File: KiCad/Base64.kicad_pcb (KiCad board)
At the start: 4 copper layers, 25.1 x 81.8 mm, 29 parts, among them J1 1473149-1, J2 Conn_01x03, U1 501MLFT, U10 68000_PinHeader, U2 SN74CBTD3861DGVR, U3 SN74CBTD3861DGVR, U4 SN74CBTD3861DGVR, U5 SN74CBTD3861DGVR, U6 SN74CBTD3861DGVR, U7 SN74CBTD3861DGVR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

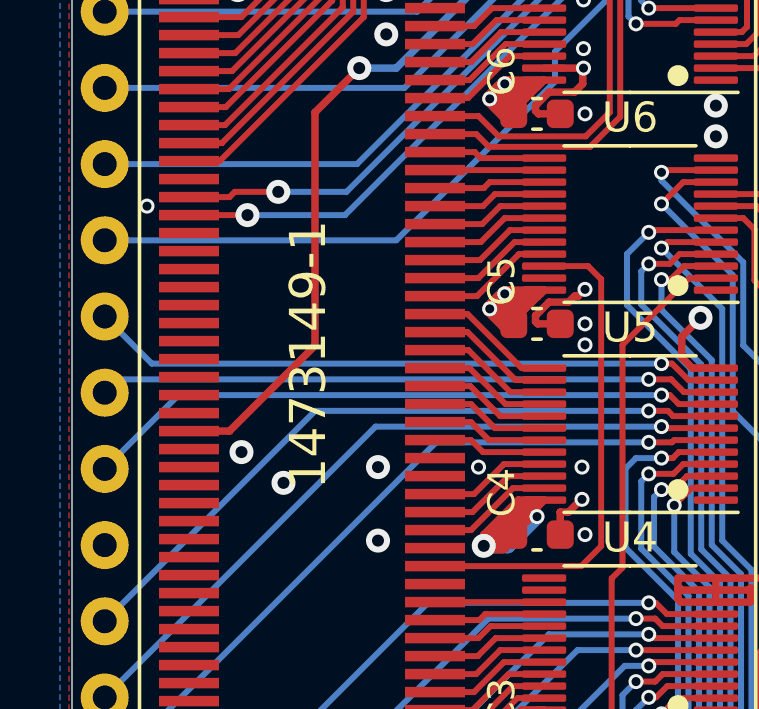
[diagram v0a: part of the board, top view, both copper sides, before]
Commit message: Change J1 value from 1473149-1 (SO-DIMM DDR) to 1473149-4 (SO-DIMM DDR2) as keying is different and iCESugar-Pro module is of DDR2 type.
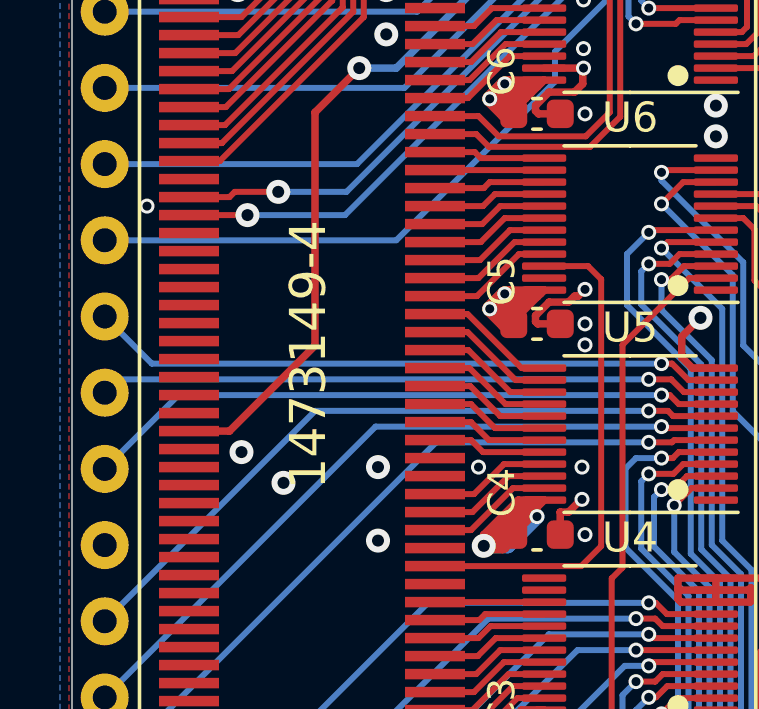
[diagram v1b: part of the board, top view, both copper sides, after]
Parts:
- J1: value 1473149-1 -> 1473149-4
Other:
- board text added: "1473149-4"
- board text removed: "1473149-1"
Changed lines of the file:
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@@
       (effects (font (size 1 1) (thickness 0.15)))
     )
-    (fp_text value 1473149-1 (at -5.6 0 90) (layer F.Fab) hide
+    (fp_text value 1473149-4 (at -5.6 0 90) (layer F.Fab) hide
       (effects (font (size 1 1) (thickness 0.15)))
     )
@@
     )
   )
-  (gr_text 1473149-1 (at 97.225 79.3 90) (layer F.SilkS)
+  (gr_text 1473149-4 (at 97.225 79.3 90) (layer F.SilkS)
     (effects (font (size 1.2 1.2) (thickness 0.2)))
   )

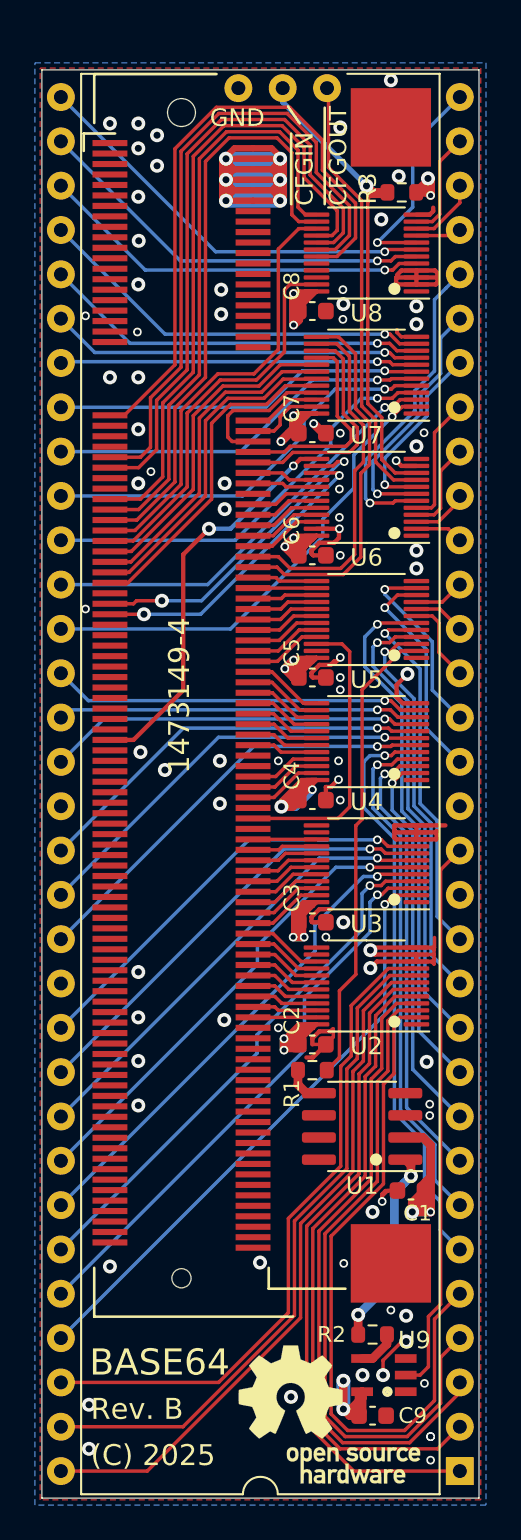
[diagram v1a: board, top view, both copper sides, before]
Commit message: Redesign with 570BLFT in order to generate a phase aligned 84 MHz clock
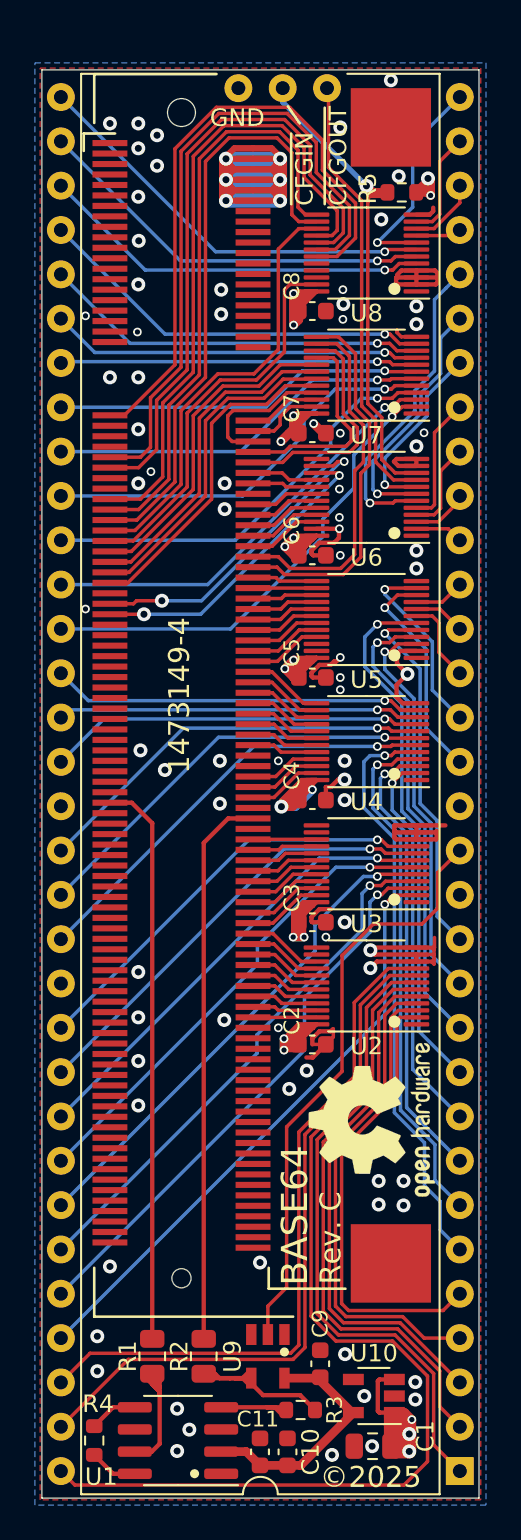
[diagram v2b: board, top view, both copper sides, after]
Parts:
- removed the REF** at (103.6, 120.5)
- added C10: 100nF, Capacitor_SMD:C_0603_1608Metric, F.Cu at (103.4, 122.7)
- added C11: 10nF, Capacitor_SMD:C_0603_1608Metric, F.Cu at (101.8, 122.7)
- added R3: 33, Resistor_SMD:R_0603_1608Metric, F.Cu at (104.2, 120.2)
- added R4: 33, Resistor_SMD:R_0603_1608Metric, F.Cu at (92.3, 122.0)
- added REF**: OSHW-Logo2_9.8x8mm_SilkScreen, Symbol:OSHW-Logo2_9.8x8mm_SilkScreen, F.Cu at (108.3, 103.6)
- added U10: TLV75533PDBVR, Package_TO_SOT_SMD:SOT-23-5, F.Cu at (108.4, 119.5)
- C1: value 10nF -> 1uF; footprint Capacitor_SMD:C_0603_1608Metric -> Capacitor_SMD:C_0805_2012Metric
- R1, R2: footprint Resistor_SMD:R_0603_1608Metric -> Resistor_SMD:R_0805_2012Metric
- U1: value 501MLFT -> 570BLFT
- U9: value 74AHCT1G17 -> SN74LVC1G17DBVR; footprint Base64:SOT95P275X110-5N -> Base64:SOT95P280X145-5N
- moved U1 20.9 mm to (97.2, 122.0)
- moved R1 18.8 mm to (95.7, 117.2), turned to 90 degrees
- moved C1 14.8 mm to (108.3, 122.3)
- moved R2 9.76 mm to (98.6, 117.2), turned to 270 degrees
- moved U9 6.74 mm to (102.3, 117.2), turned to 270 degrees
- moved C9 4.23 mm to (105.3, 117.6), turned to 90 degrees
- renumbered R3 to R5, U10 to U11
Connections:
- net Net-(U1-Pad6) renamed /S0
- C9 pad 1: VCC -> 3V3
- J1 pad 115: PL26A -> 12x_CLK
- J1 pad 118: PT27A -> CLK
- R1 pad 1: Net-(R1-Pad1) -> /CLKx12
- R1 pad 2: 2xCLK -> 12x_CLK
- R2 pad 1: /CLK_BUF -> CLK
- R2 pad 2: CLK -> /CLK_BUF
- U1 pad 1: CLK -> /S1
- U1 pad 2: VCC -> 3V3
- U1 pad 4: Net-(U1-Pad4) -> ICLK
- U1 pad 5: Net-(R1-Pad1) -> /FBIN
- U1 pad 7: Net-(U1-Pad7) -> /CLKx12
- U1 pad 8: Net-(U1-Pad8) -> /CLKx6
- U5 pad 2: 2xCLK -> GND
- U5 pad 22: PT27A -> Net-(U5-Pad22)
- U6 pad 11: CLK -> GND
- U6 pad 13: PL23A -> Net-(U6-Pad13)
- U9 pad 5: VCC -> 3V3
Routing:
- net 12x_CLK: track 0.00 -> 32.5 mm
- net 2xCLK: track 26.7 -> 0.00 mm
- net CLK: track 56.4 -> 31.8 mm, vias 3 -> 0
- net PL23A: track 23.1 -> 0.00 mm, vias 2 -> 0
- net D5: track 40.2 -> 57.4 mm
- net PT27A: track 16.8 -> 0.00 mm
- net 3V3: track 0.00 -> 14.1 mm
- net D0: track 39.1 -> 26.1 mm
- net D1: track 38.1 -> 27.4 mm
- net /CLKx12: track 0.00 -> 9.79 mm
- net /CLK_BUF: track 2.32 -> 11.7 mm
- net VCC: track 160.9 -> 152.4 mm, vias 26 -> 25
- net D2: track 37.2 -> 29.4 mm
- net ICLK: track 0.00 -> 5.32 mm
- net D3: track 37.1 -> 32.7 mm
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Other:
- board text added: "Rev. C"
- board text added: "©2025"
- board text removed: "(C) 2025"
- board text removed: "Rev. B"

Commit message: Improve via GND-stitching around U1 and remove JLCJLCJLCJLC silkscreen label
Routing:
- net VCC: track 152.4 -> 155.2 mm
- net GND: vias 80 -> 82
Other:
- board text removed: "JLCJLCJLCJLC"
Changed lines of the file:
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@@
   (general
     (thickness 1.6)
-    (drawings 19)
-    (tracks 1255)
+    (drawings 18)
+    (tracks 1262)
     (zones 0)
     (modules 34)
@@
     (effects (font (size 1.2 1.2) (thickness 0.2)))
   )
-  (gr_text JLCJLCJLCJLC (at 110.55 94.225 270) (layer B.SilkS)
-    (effects (font (size 1.2 1.2) (thickness 0.15)) (justify mirror))
-  )
   (gr_text ~CFGOUT (at 105.1 51.7 270) (layer B.SilkS)
     (effects (font (size 1 1) (thickness 0.15)) (justify left mirror))
@@
   (segment (start 109.7 76.930344) (end 109.7 77.475) (width 0.25) (layer F.Cu) (net 1))
   (via (at 106.725 117.05) (size 0.8) (drill 0.4) (layers F.Cu B.Cu) (net 1))
+  (via (at 102.15 120.825) (size 0.8) (drill 0.4) (layers F.Cu B.Cu) (net 1))
+  (via (at 104.275 121.125) (size 0.8) (drill 0.4) (layers F.Cu B.Cu) (net 1))
   (via (at 110.55 120.8) (size 0.5) (drill 0.3) (layers F.Cu B.Cu) (net 2))
   (via (at 110.4 121.625) (size 0.8) (drill 0.4) (layers F.Cu B.Cu) (net 2))
@@
   (segment (start 109.775 120.4) (end 109.475 120.4) (width 0.5) (layer F.Cu) (net 2))
   (segment (start 110.4 121.025) (end 109.775 120.4) (width 0.5) (layer F.Cu) (net 2))
+  (segment (start 110.4 122.625) (end 110.4 121.625) (width 0.8) (layer B.Cu) (net 2))
+  (segment (start 110.55 121.475) (end 110.4 121.625) (width 0.5) (layer B.Cu) (net 2))
+  (segment (start 110.55 120.8) (end 110.55 121.475) (width 0.5) (layer B.Cu) (net 2))
+  (segment (start 110.4 120.95) (end 110.55 120.8) (width 0.5) (layer B.Cu) (net 2))
+  (segment (start 110.4 121.625) (end 110.4 120.95) (width 0.5) (layer B.Cu) (net 2))
   (via (at 108.575 53.35) (size 0.5) (drill 0.3) (layers F.Cu B.Cu) (net 3))
   (segment (start 110.8125 53.35) (end 108.575 53.35) (width 0.2) (layer F.Cu) (net 3))
